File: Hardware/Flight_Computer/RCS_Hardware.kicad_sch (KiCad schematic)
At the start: 55 parts, among them J1 SWD, J2 TYPE-C-31-M-12, J3 SPI, J4 5V, J5 GND, J6 Solenoids, J7 SPI, J8 Conn_01x05_Male, U1 STM32F401CCU6, U2 AMS1117-3.3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

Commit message: removed RCS-specific components
removed solenoid connectors, SPI connectors, LTC, and extra IMU
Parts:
- removed C21, C24: 0.1uF, Capacitor_SMD:C_0402_1005Metric, symbol Device:C
- removed C22: 2.2nF, Capacitor_SMD:C_0402_1005Metric, symbol Device:C
- removed C23: 100nF, Capacitor_SMD:C_0402_1005Metric, symbol Device:C
- removed C25: 10nF, Capacitor_SMD:C_0402_1005Metric, symbol Device:C
- removed J3, J7: SPI, Connector_PinHeader_2.54mm:PinHeader_1x08_P2.54mm_Vertical, symbol Connector:Conn_01x08_Pin
- removed J6: Solenoids, Connector_PinHeader_2.54mm:PinHeader_1x07_P2.54mm_Vertical, symbol Connector:Conn_01x07_Male
- removed J8: Conn_01x05_Male, Connector_PinHeader_2.54mm:PinHeader_1x05_P2.54mm_Vertical, symbol Connector:Conn_01x05_Male
- removed U6: MPU-6050, Sensor_Motion:InvenSense_QFN-24_4x4mm_P0.5mm, symbol Sensor_Motion:MPU-6050
- removed U7: LTC1690N8, LTC1690N8:LTC1690N8, symbol lt1690n8:LT1690N8
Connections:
- net RX: no longer names the net of U1.12 (PA2)
- net S1: no longer names the net of U1.11 (PA1)
- net S2: no longer names the net of U1.19 (PB1)
- net S3: no longer names the net of U1.21 (PB10)
- net S4: no longer names the net of U1.26 (PB13)
- net S5: no longer names the net of U1.27 (PB14)
- net S6: no longer names the net of U1.28 (PB15)
- net TX: no longer names the net of U1.13 (PA3)
- no-connect marks 21 -> 30
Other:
- note added: "Altimeter"
- note added: "GPS"
- note added: "UART (TO MOTOR CONTROLLER)"
- moved on the sheet: C20, J4, J5, R7, U5

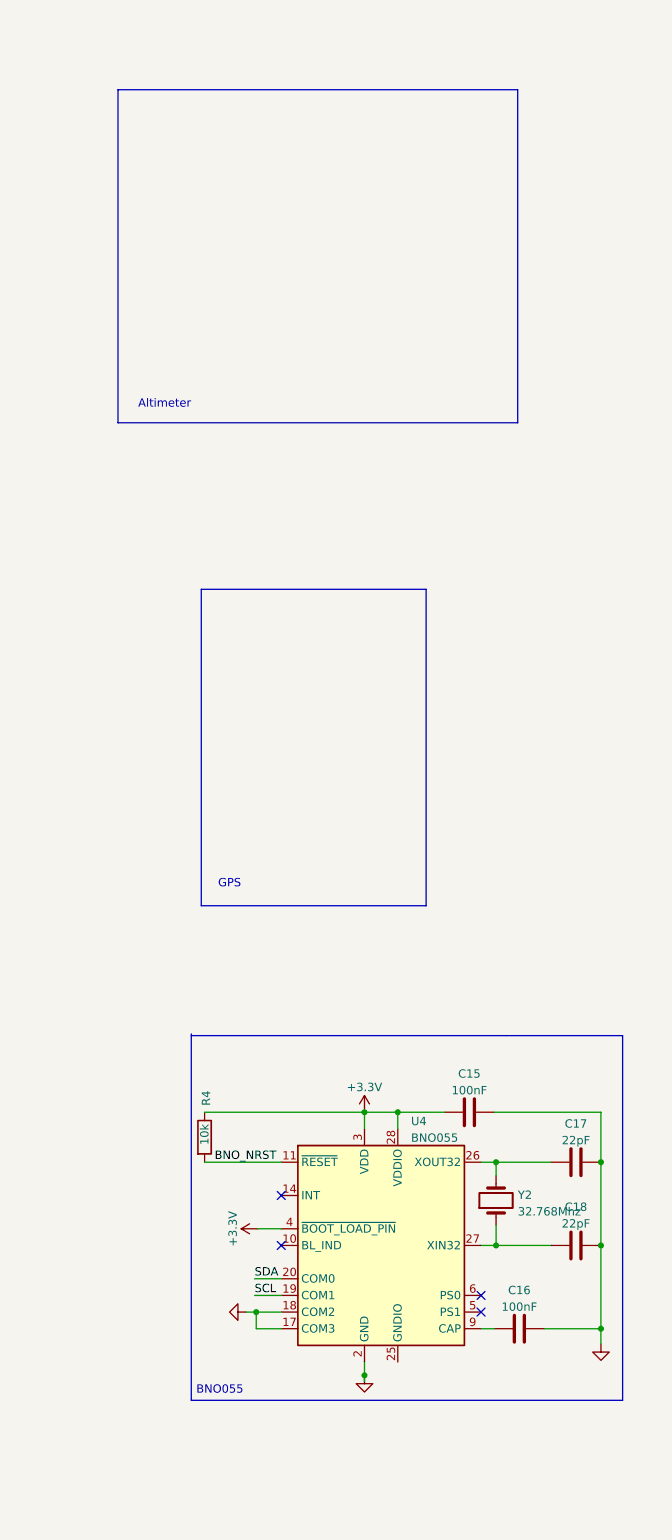
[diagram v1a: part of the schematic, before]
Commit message: Added GPS and Altimeter to schematic
still need to add wires
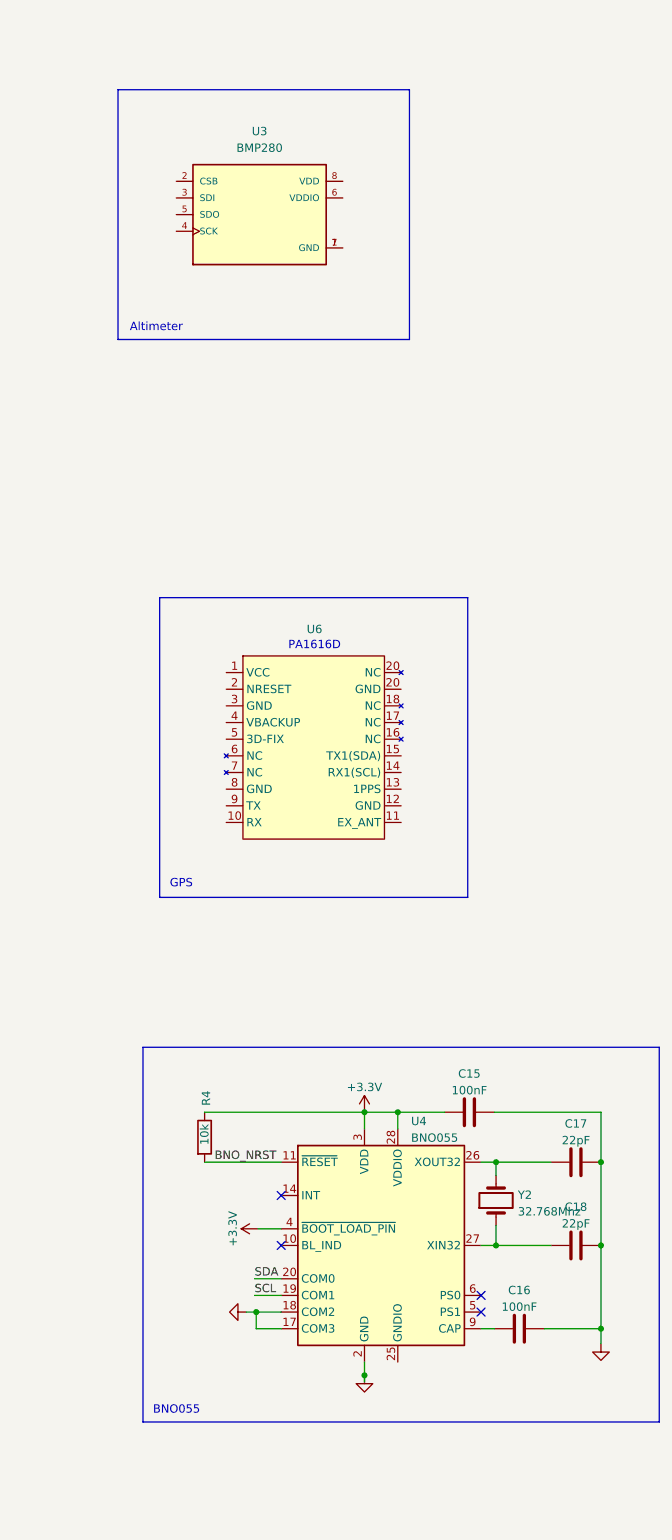
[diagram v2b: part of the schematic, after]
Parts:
- added U3: BMP280, XDCR_BMP280, symbol BMP280:BMP280
- added U6: ~, symbol PA1616D:PA1616D
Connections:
- new net: U3.1 (GND), U3.7 (GND)
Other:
- note added: "PA1616D"
